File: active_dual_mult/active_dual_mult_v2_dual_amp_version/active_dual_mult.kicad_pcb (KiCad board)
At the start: 2 copper layers, 15.3 x 109.6 mm, 33 parts, among them J1 EURO_HEADER_10pin, J10 B3Out, J11 B4Out, J2 AIn, J3 A1Out, J4 A2Out, J5 A3Out, J6 A4Out, J7 BIn, J8 B1Out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

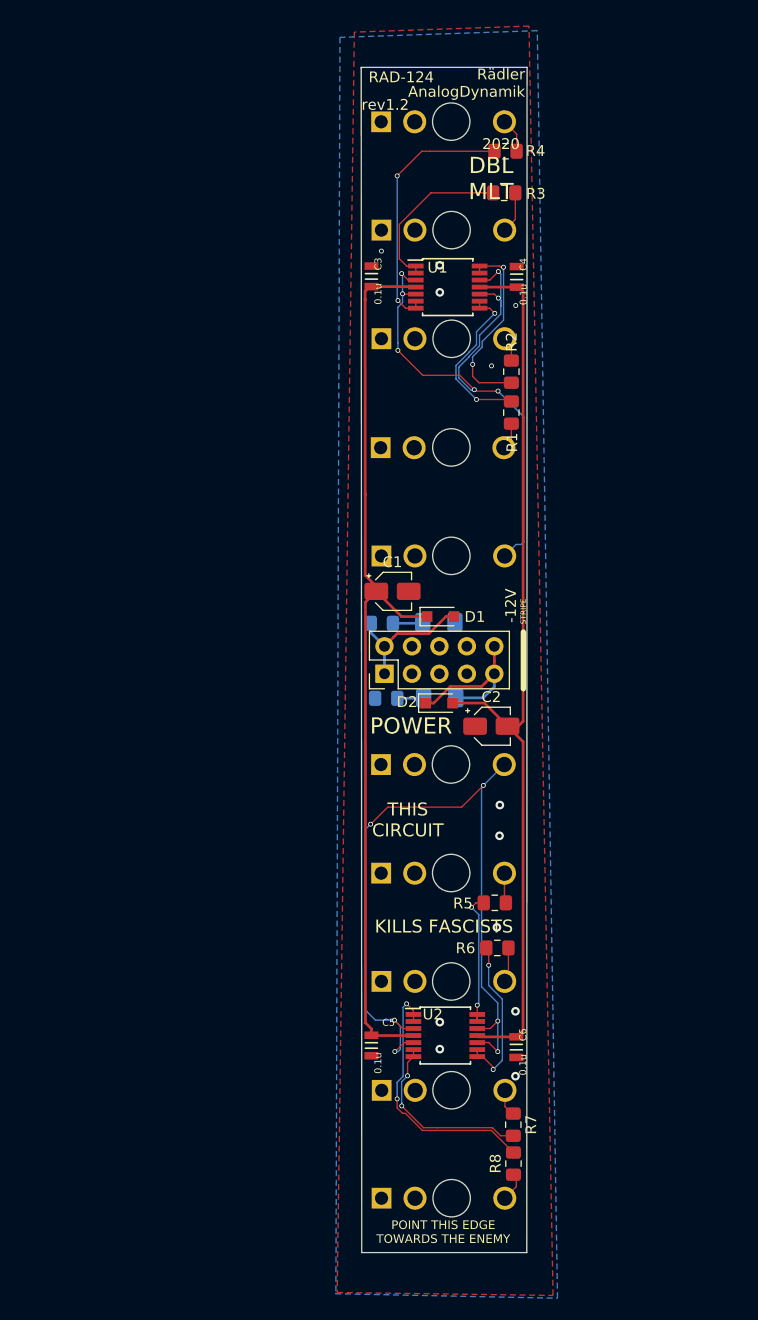
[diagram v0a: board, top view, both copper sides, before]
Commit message: Rewired PCB in version 2 of RAD124 to leverage dual op-amp packages and minimize number of vias for output channels. Changed op amps to OPA2174 SOIC packages to improve unity-gain stability and reduce phase-inversion problems found in TL07X series op amps.
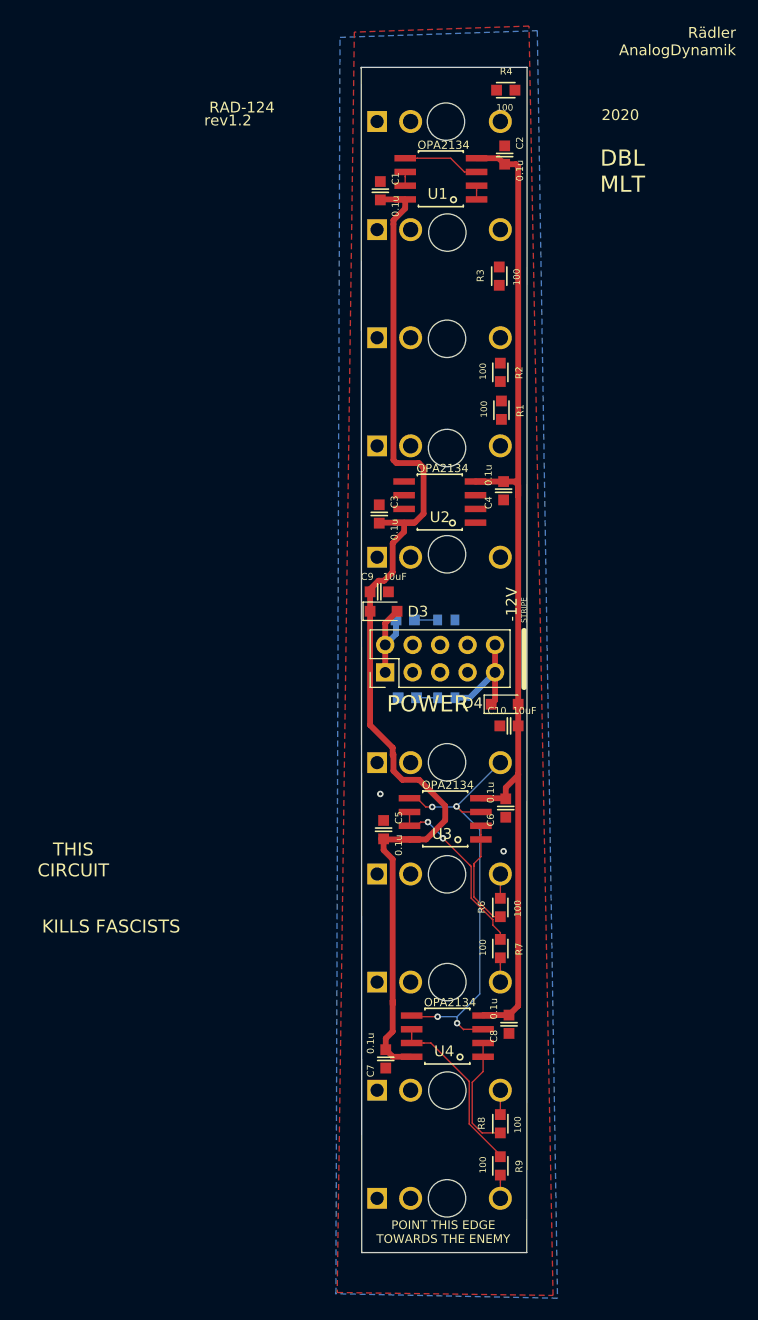
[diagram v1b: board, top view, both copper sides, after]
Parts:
- removed the C1 at (155.6, 70.2)
- removed the C2 at (164.8, 82.6)
- added C10: 10uF, 4ms_Capacitor:C_0603, F.Cu at (166.4, 82.6)
- added C3: 0.1u, 4ms_Capacitor:C_0603, F.Cu at (154.4, 63.0)
- added C4: 0.1u, 4ms_Capacitor:C_0603, F.Cu at (165.9, 60.9)
- added C7: 0.1u, 4ms_Capacitor:C_0603, F.Cu at (155.0, 113.4)
- added C8: 0.1u, 4ms_Capacitor:C_0603, F.Cu at (166.4, 110.2)
- added C9: 10uF, 4ms_Capacitor:C_0603, F.Cu at (154.4, 70.2)
- added U3: OPA2134, 4ms_Package_SOIC:SOIC-8_5.28x4.9mm_Pitch1.27mm, F.Cu at (160.5, 91.2)
- added U4: OPA2134, 4ms_Package_SOIC:SOIC-8_5.28x4.9mm_Pitch1.27mm, F.Cu at (160.7, 111.3)
- C1: renamed from C3; footprint 4ms_Capacitor:C_0805 -> 4ms_Capacitor:C_0603
- C2: renamed from C4; footprint 4ms_Capacitor:C_0805 -> 4ms_Capacitor:C_0603
- C5, C6: footprint 4ms_Capacitor:C_0805 -> 4ms_Capacitor:C_0603
- D1: renamed from D3; footprint LED_SMD:LED_1206_3216Metric_Pad1.42x1.75mm_HandSolder -> 4ms_LED:LED_0603_1608Metric
- D2: renamed from D4; footprint LED_SMD:LED_1206_3216Metric_Pad1.42x1.75mm_HandSolder -> 4ms_LED:LED_0603_1608Metric
- R1, R10, R2, R3, R4: footprint Resistor_SMD:R_0805_2012Metric_Pad1.15x1.40mm_HandSolder -> 4ms_Resistor:R_0603
- R5: renamed from R9; footprint Resistor_SMD:R_0805_2012Metric_Pad1.15x1.40mm_HandSolder -> 4ms_Resistor:R_0603
- R6: renamed from R5; footprint Resistor_SMD:R_0805_2012Metric_Pad1.15x1.40mm_HandSolder -> 4ms_Resistor:R_0603
- R7: renamed from R6; footprint Resistor_SMD:R_0805_2012Metric_Pad1.15x1.40mm_HandSolder -> 4ms_Resistor:R_0603
- R8: renamed from R7; footprint Resistor_SMD:R_0805_2012Metric_Pad1.15x1.40mm_HandSolder -> 4ms_Resistor:R_0603
- R9: renamed from R8; footprint Resistor_SMD:R_0805_2012Metric_Pad1.15x1.40mm_HandSolder -> 4ms_Resistor:R_0603
- U1, U2: value TL074 -> OPA2134; footprint Package_SO:TSSOP-14_4.4x5mm_P0.65mm -> 4ms_Package_SOIC:SOIC-8_5.28x4.9mm_Pitch1.27mm
- moved U2 49.3 mm to (160.0, 61.9), turned to 180 degrees
- moved C6 22.1 mm to (166.1, 90.2), turned to 90 degrees
- moved C5 20.0 mm to (154.8, 92.2)
- moved C2 11.3 mm to (166.0, 29.8)
- moved U1 10.0 mm to (160.1, 32.0), turned to 180 degrees
- moved C1 7.96 mm to (154.5, 33.1)
- moved R3 7.71 mm to (165.5, 41.0), turned to 270 degrees
- moved D4 6.06 mm to (166.0, 80.6)
- moved R4 5.65 mm to (166.1, 23.8)
- moved D3 5.29 mm to (154.8, 72.0)
- moved R5 2.18 mm to (156.8, 72.8)
- moved R10 1.96 mm to (157.0, 80.0)
- moved R9 1.23 mm to (165.6, 123.3)
- moved R8 1.20 mm to (165.6, 119.4)
- moved R2 1.02 mm to (165.6, 49.9), turned to 90 degrees
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- renumbered D1 to D3, D2 to D4, J2 to J1, J1 to J2
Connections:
- C5 pad 1: VCC -> GND
- C5 pad 2: GND -> VCC
- C6 pad 1: VEE -> GND
- C6 pad 2: GND -> VEE
- R6 pad 2: Net-(R5-Pad2) -> Net-(R6-Pad2)
- R7 pad 2: Net-(R6-Pad2) -> Net-(R7-Pad2)
- R8 pad 2: Net-(R7-Pad2) -> Net-(R8-Pad2)
- R9 pad 2: Net-(R8-Pad2) -> Net-(R9-Pad2)
- U1 pad 1: Net-(R3-Pad2) -> Net-(R1-Pad2)
- U1 pad 2: Net-(R3-Pad2) -> Net-(R1-Pad2)
- U1 pad 4: VCC -> VEE
- U1 pad 6: Net-(R4-Pad2) -> Net-(R2-Pad2)
- U1 pad 7: Net-(R4-Pad2) -> Net-(R2-Pad2)
- U1 pad 8: Net-(R1-Pad2) -> VCC
- U2 pad 1: Net-(R8-Pad2) -> Net-(R3-Pad2)
- U2 pad 2: Net-(R8-Pad2) -> Net-(R3-Pad2)
- U2 pad 3: /BIn -> /AIn
- U2 pad 4: VCC -> VEE
- U2 pad 5: /BIn -> /AIn
- U2 pad 6: Net-(R7-Pad2) -> Net-(R4-Pad2)
- U2 pad 7: Net-(R7-Pad2) -> Net-(R4-Pad2)
- U2 pad 8: Net-(R6-Pad2) -> VCC
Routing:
- net /AIn: track 56.4 -> 7.13 mm, vias 7 -> 0
- net /BIn: track 72.8 -> 41.6 mm, vias 6 -> 4
- net Net-(R4-Pad2): track 24.1 -> 0.00 mm, vias 2 -> 0
- net VCC: track 84.5 -> 102.5 mm
- net Net-(R2-Pad2): track 18.5 -> 1.27 mm, vias 2 -> 0
- net Net-(R9-Pad2): track 0.00 -> 16.2 mm
- net Net-(R3-Pad2): track 15.5 -> 0.00 mm
- net Net-(R1-Pad2): track 15.8 -> 1.27 mm, vias 2 -> 0
- net Net-(R8-Pad2): track 24.9 -> 10.8 mm, vias 2 -> 0
- net Net-(R5-Pad2): track 12.8 -> 0.00 mm, vias 2 -> 0
- net VEE: track 84.8 -> 95.6 mm
- net -12V: track 15.2 -> 10.3 mm
- net Net-(R6-Pad2): track 15.0 -> 10.9 mm, vias 2 -> 0
- net +12V: track 12.8 -> 8.83 mm
- net /A3Out: track 3.85 -> 0.00 mm
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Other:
- outline, holes or cut-outs redrawn
- net class PWR: clearance 0.127 -> 0.254; trace_width 0.254 -> 0.54; via_dia 0.54 -> 0.8; via_drill 0.3 -> 0.6
- net class SIGNAL: via_dia 0.45 -> 0.6
